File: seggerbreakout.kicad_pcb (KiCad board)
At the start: 2 copper layers, 29.5 x 28 mm, 4 parts, among them P1 SWD, P2 JTAG, P3 JTAG

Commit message: Add a SWD guide (incorrect for now due to upside down reading of segger docs)
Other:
- board text added: "1"
- board text added: "10"
- board text added: "2"
- board text added: "3"
- board text added: "4"
- board text added: "5"
- board text added: "5v*"
- board text added: "6"
- board text added: "7"
- board text added: "8"
- board text added: "9"
- board text added: "IDT"
- board text added: "J-LINK Breakout w/SWD"
- board text added: "NC"
- board text added: "RESET"
- board text added: "RTCK"
- board text added: "TCK"
- board text added: "TDD"
- board text added: "TMS"
- board text added: "VTref"
- board text added: "nTRST"
- board text removed: "J-LINK Breakout+SWD"
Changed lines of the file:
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@@
   (general
     (links 37)
-    (no_connects 0)
-    (area 175.27905 114.554 221.03715 160.95345)
+    (no_connects 18)
+    (area 175.27905 114.554 221.90075 160.95345)
     (thickness 1.6)
-    (drawings 73)
+    (drawings 114)
     (tracks 83)
     (zones 0)
@@
     (pad_to_mask_clearance 0)
     (aux_axis_origin 0 0)
-    (visible_elements FFFFFFBF)
+    (visible_elements FFFF7FFF)
     (pcbplotparams
       (layerselection 284196865)
@@
       (xy -1.21158 1.79578)) (layer F.SilkS) (width 0.00254))
   )
+  (gr_text SWD (at 211.836 120.904 90) (layer B.SilkS)
+    (effects (font (size 0.75 0.75) (thickness 0.125)) (justify mirror))
+  )
+  (gr_line (start 186.944 126.0475) (end 186.944 126.8095) (angle 90) (layer B.SilkS) (width 0.2))
+  (gr_line (start 190.0555 133.477) (end 190.0555 133.731) (angle 90) (layer B.SilkS) (width 0.2))
+  (gr_text NC (at 186.944 124.6505 270) (layer B.SilkS)
+    (effects (font (size 1.524 1.016) (thickness 0.254)) (justify mirror))
+  )
+  (gr_text 9 (at 209.4865 122.7455) (layer B.SilkS)
+    (effects (font (size 0.5 0.5) (thickness 0.125)) (justify mirror))
+  )
+  (gr_text 10 (at 209.4865 119.1895) (layer B.SilkS)
+    (effects (font (size 0.5 0.5) (thickness 0.125)) (justify mirror))
+  )
+  (gr_text 7 (at 206.883 122.7455) (layer B.SilkS)
+    (effects (font (size 0.5 0.5) (thickness 0.125)) (justify mirror))
+  )
+  (gr_text 8 (at 206.883 119.1895) (layer B.SilkS)
+    (effects (font (size 0.5 0.5) (thickness 0.125)) (justify mirror))
+  )
+  (gr_text 6 (at 204.216 119.1895) (layer B.SilkS)
+    (effects (font (size 0.5 0.5) (thickness 0.125)) (justify mirror))
+  )
+  (gr_text 5 (at 204.1525 122.7455) (layer B.SilkS)
+    (effects (font (size 0.5 0.5) (thickness 0.125)) (justify mirror))
+  )
+  (gr_text 3 (at 201.4855 122.7455) (layer B.SilkS)
+    (effects (font (size 0.5 0.5) (thickness 0.125)) (justify mirror))
+  )
+  (gr_text 4 (at 201.4855 119.1895) (layer B.SilkS)
+    (effects (font (size 0.5 0.5) (thickness 0.125)) (justify mirror))
+  )
+  (gr_text 2 (at 198.8185 119.1895) (layer B.SilkS)
+    (effects (font (size 0.5 0.5) (thickness 0.125)) (justify mirror))
+  )
+  (gr_text 1 (at 198.8185 122.7455) (layer B.SilkS)
+    (effects (font (size 0.5 0.5) (thickness 0.125)) (justify mirror))
+  )
+  (gr_line (start 210.82 120.904) (end 197.485 120.904) (angle 90) (layer B.SilkS) (width 0.2))
+  (gr_line (start 197.485 122.047) (end 200.152 122.047) (angle 90) (layer B.SilkS) (width 0.2))
+  (gr_line (start 197.485 119.761) (end 197.485 122.047) (angle 90) (layer B.SilkS) (width 0.2))
+  (gr_line (start 200.152 119.761) (end 197.485 119.761) (angle 90) (layer B.SilkS) (width 0.2))
+  (gr_line (start 200.152 122.047) (end 202.819 122.047) (angle 90) (layer B.SilkS) (width 0.2))
+  (gr_line (start 200.152 119.761) (end 200.152 122.047) (angle 90) (layer B.SilkS) (width 0.2))
+  (gr_line (start 202.819 119.761) (end 200.152 119.761) (angle 90) (layer B.SilkS) (width 0.2))
+  (gr_line (start 202.819 122.047) (end 205.486 122.047) (angle 90) (layer B.SilkS) (width 0.2))
+  (gr_line (start 202.819 119.761) (end 202.819 122.047) (angle 90) (layer B.SilkS) (width 0.2))
+  (gr_line (start 205.486 119.761) (end 202.819 119.761) (angle 90) (layer B.SilkS) (width 0.2))
+  (gr_line (start 205.486 122.047) (end 208.153 122.047) (angle 90) (layer B.SilkS) (width 0.2))
+  (gr_line (start 205.486 119.761) (end 205.486 122.047) (angle 90) (layer B.SilkS) (width 0.2))
+  (gr_line (start 208.153 119.761) (end 205.486 119.761) (angle 90) (layer B.SilkS) (width 0.2))
+  (gr_line (start 208.153 119.761) (end 208.153 120.904) (angle 90) (layer B.SilkS) (width 0.2))
+  (gr_line (start 210.82 119.761) (end 208.153 119.761) (angle 90) (layer B.SilkS) (width 0.2))
+  (gr_line (start 210.82 120.904) (end 210.82 119.761) (angle 90) (layer B.SilkS) (width 0.2))
+  (gr_line (start 208.153 120.904) (end 208.153 122.047) (angle 90) (layer B.SilkS) (width 0.2))
+  (gr_line (start 210.82 122.047) (end 210.82 120.904) (angle 90) (layer B.SilkS) (width 0.2))
+  (gr_line (start 208.153 122.047) (end 210.82 122.047) (angle 90) (layer B.SilkS) (width 0.2))
+  (gr_text nTRST (at 209.55 121.539) (layer B.SilkS)
+    (effects (font (size 0.5 0.5) (thickness 0.125)) (justify mirror))
+  )
+  (gr_text RTCK (at 206.756 121.539) (layer B.SilkS)
+    (effects (font (size 0.5 0.5) (thickness 0.125)) (justify mirror))
+  )
+  (gr_text 5v* (at 204.216 121.539) (layer B.SilkS)
+    (effects (font (size 0.5 0.5) (thickness 0.125)) (justify mirror))
+  )
+  (gr_text GND (at 201.4855 121.539) (layer B.SilkS)
+    (effects (font (size 0.5 0.5) (thickness 0.125)) (justify mirror))
+  )
+  (gr_text VTref (at 198.882 121.539) (layer B.SilkS)
+    (effects (font (size 0.5 0.5) (thickness 0.125)) (justify mirror))
+  )
+  (gr_text RESET (at 209.55 120.396) (layer B.SilkS)
+    (effects (font (size 0.5 0.5) (thickness 0.125)) (justify mirror))
+  )
+  (gr_text IDT (at 206.756 120.396) (layer B.SilkS)
+    (effects (font (size 0.5 0.5) (thickness 0.125)) (justify mirror))
+  )
+  (gr_text TDD (at 204.216 120.396) (layer B.SilkS)
+    (effects (font (size 0.5 0.5) (thickness 0.125)) (justify mirror))
+  )
+  (gr_text TCK (at 201.4855 120.396) (layer B.SilkS)
+    (effects (font (size 0.5 0.5) (thickness 0.125)) (justify mirror))
+  )
+  (gr_text TMS (at 198.882 120.396) (layer B.SilkS)
+    (effects (font (size 0.5 0.5) (thickness 0.125)) (justify mirror))
+  )
   (gr_text 2014-09-12 (at 198.374 145.288) (layer B.SilkS)
     (effects (font (size 1.0668 1.0668) (thickness 0.2667)) (justify mirror))
   )
-  (gr_text "J-LINK Breakout+SWD\n" (at 211.836 132.588 270) (layer B.SilkS)
+  (gr_text "J-LINK Breakout w/SWD\n" (at 211.836 132.588 270) (layer B.SilkS)
     (effects (font (size 1.0668 1.0668) (thickness 0.2667)) (justify mirror))
   )
-  (gr_line (start 208.5975 126.0475) (end 208.5975 125.222) (angle 90) (layer B.SilkS) (width 0.2))
   (gr_line (start 199.92975 134.20725) (end 199.92975 134.46125) (angle 90) (layer B.SilkS) (width 0.2))
   (gr_line (start 204.75575 133.69925) (end 204.75575 132.68325) (angle 90) (layer B.SilkS) (width 0.2))
@@
     (effects (font (size 1.016 1.016) (thickness 0.254)))
   )
-  (gr_text GND (at 208.534 122.428 270) (layer B.SilkS)
+  (gr_text GND (at 203.0095 124.7775) (layer B.SilkS)
     (effects (font (size 1.5 1.5) (thickness 0.3)) (justify mirror))
   )
@@
   (gr_line (start 186.97575 132.93725) (end 186.97575 132.68325) (angle 90) (layer B.SilkS) (width 0.2))
   (gr_line (start 187.73775 133.95325) (end 187.73775 134.46125) (angle 90) (layer B.SilkS) (width 0.2))
-  (gr_line (start 190.02375 133.44525) (end 190.02375 133.95325) (angle 90) (layer B.SilkS) (width 0.2))
   (gr_line (start 189.51575 132.93725) (end 189.51575 132.68325) (angle 90) (layer B.SilkS) (width 0.2))
   (gr_line (start 192.05575 132.93725) (end 192.05575 132.68325) (angle 90) (layer B.SilkS) (width 0.2))

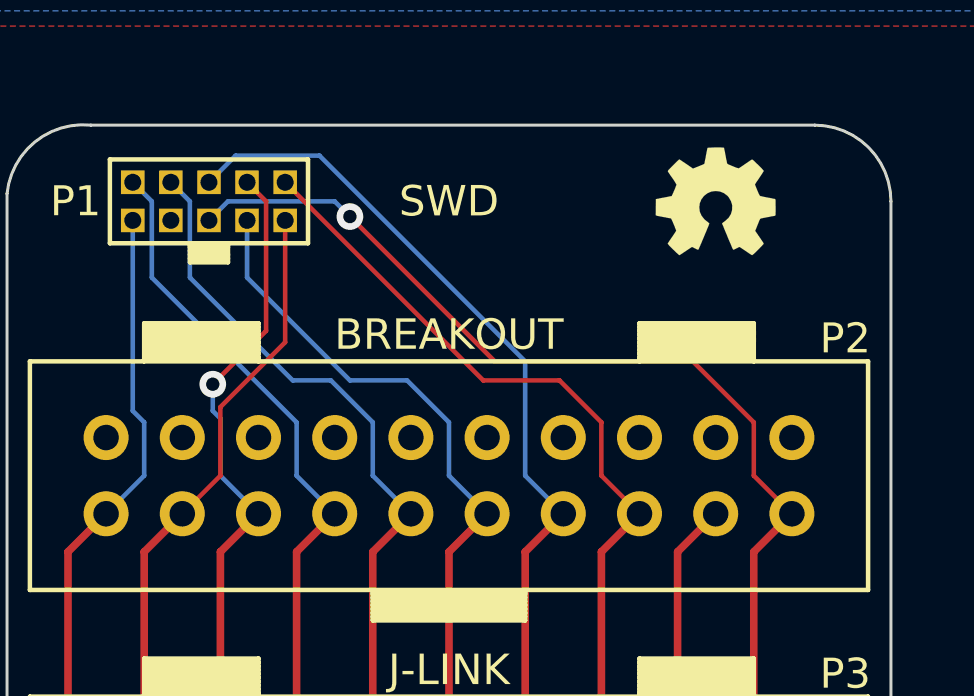
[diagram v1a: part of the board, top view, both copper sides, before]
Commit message: Update SWD pinout guide and correct schematics to be proper
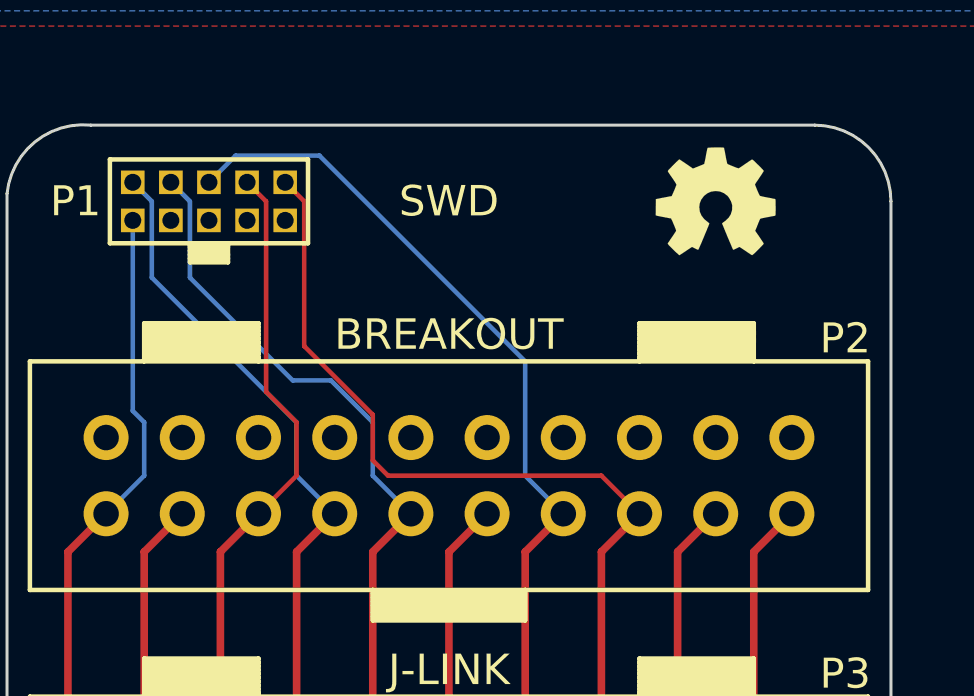
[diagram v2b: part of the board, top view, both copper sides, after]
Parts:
- P1: footprint JTAG_SMALL -> SWD
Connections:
- P1 pad 5: /5V -> GND
- P1 pad 7: /RTCK -> (no net)
- P1 pad 9: /nTRST -> GND
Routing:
- net /5V: track 37.3 -> 12.2 mm, vias 1 -> 0
- net /RTCK: track 26.4 -> 12.2 mm
- net /nTRST: track 23.4 -> 12.2 mm
- net /RESET: track 29.7 -> 32.3 mm
- net /TDI: track 24.9 -> 24.5 mm, vias 1 -> 0
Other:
- board text added: "KEY"
- board text added: "SWCLK"
- board text added: "SWDIO"
- board text added: "SWO"
- board text added: "TDI"
- board text added: "VCC"
- board text removed: "5v*"
- board text removed: "IDT"
- board text removed: "RTCK"
- board text removed: "TCK"
- board text removed: "TDD"
- board text removed: "TMS"
- board text removed: "VTref"
- board text removed: "nTRST"

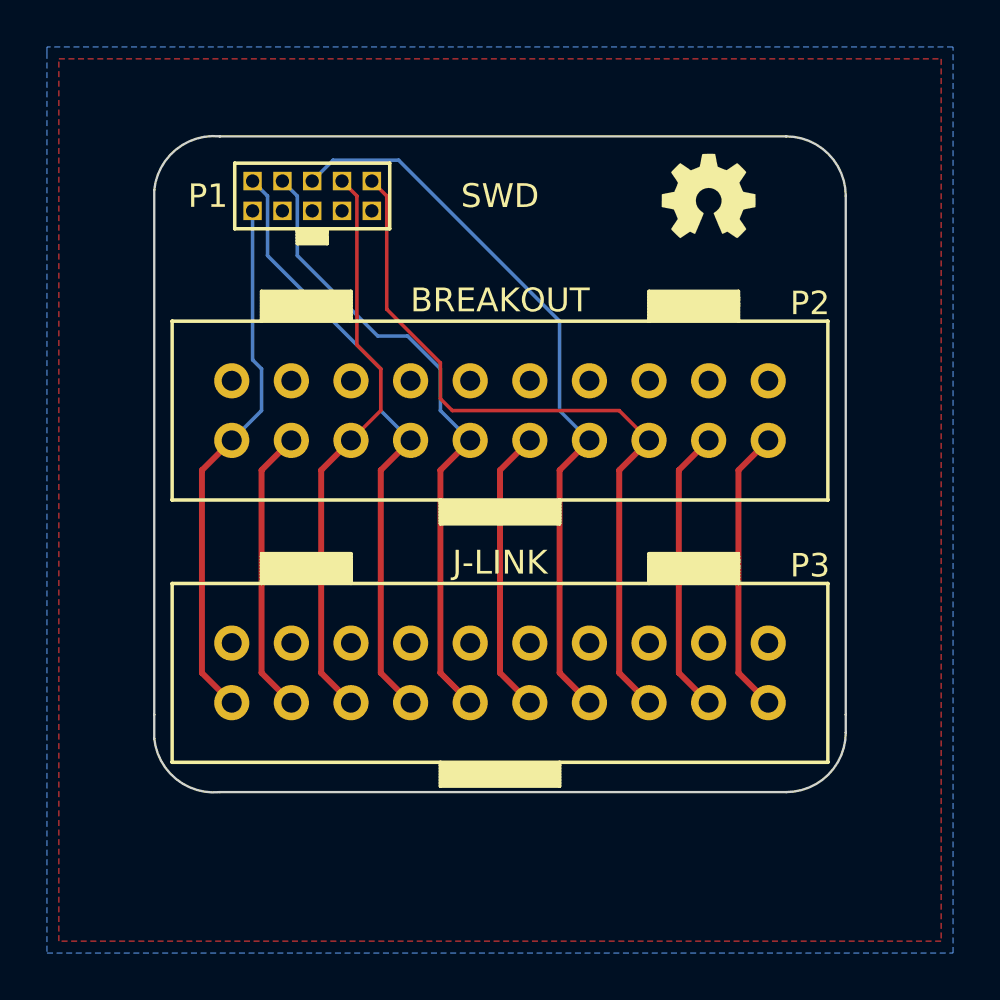
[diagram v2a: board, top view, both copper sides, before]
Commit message: Add front-side silkscreen for segger breakout
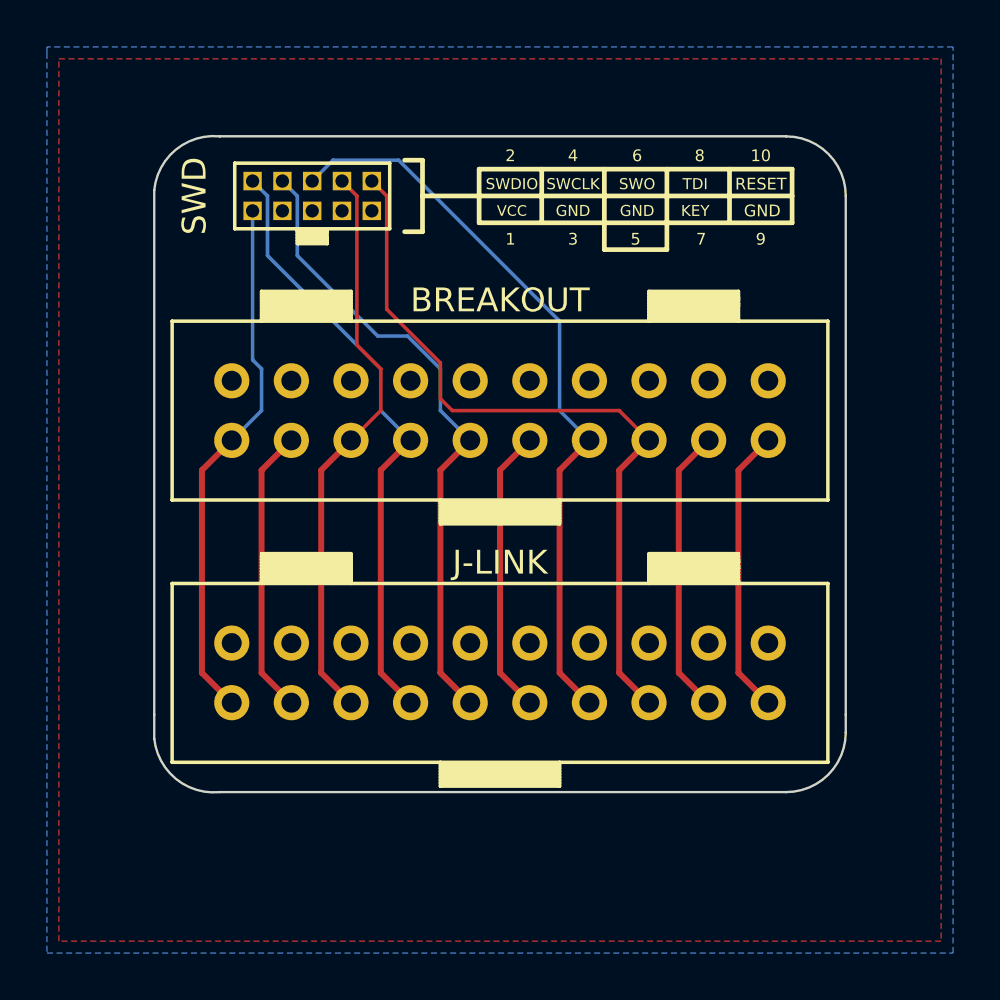
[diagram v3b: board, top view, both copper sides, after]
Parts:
- G***: footprint OSHW-logo_silkscreen_4mm -> OSHW-logo_silkscreen_2mm; moved to B.Cu
- moved G*** 31.8 mm to (184.8, 143.4), turned to 270 degrees
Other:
- board text added: "2014-10-01"
- board text added: "5V"
- board text added: "DBGRQ"
- board text added: "RTCK"
- board text added: "TCK"
- board text added: "TDO"
- board text added: "TMS"
- board text added: "VTref"
- board text added: "nTRST"
- board text removed: "2014-09-12"
- board text removed: "5V DBGRQ RESET TDO RTCK TCK TMS TDI nTRST VTref"
